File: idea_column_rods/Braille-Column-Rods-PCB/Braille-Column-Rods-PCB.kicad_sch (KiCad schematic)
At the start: 6 parts, among them J1 Conn_01x03, J5 Screw_Terminal_01x02, J6 Screw_Terminal_01x02

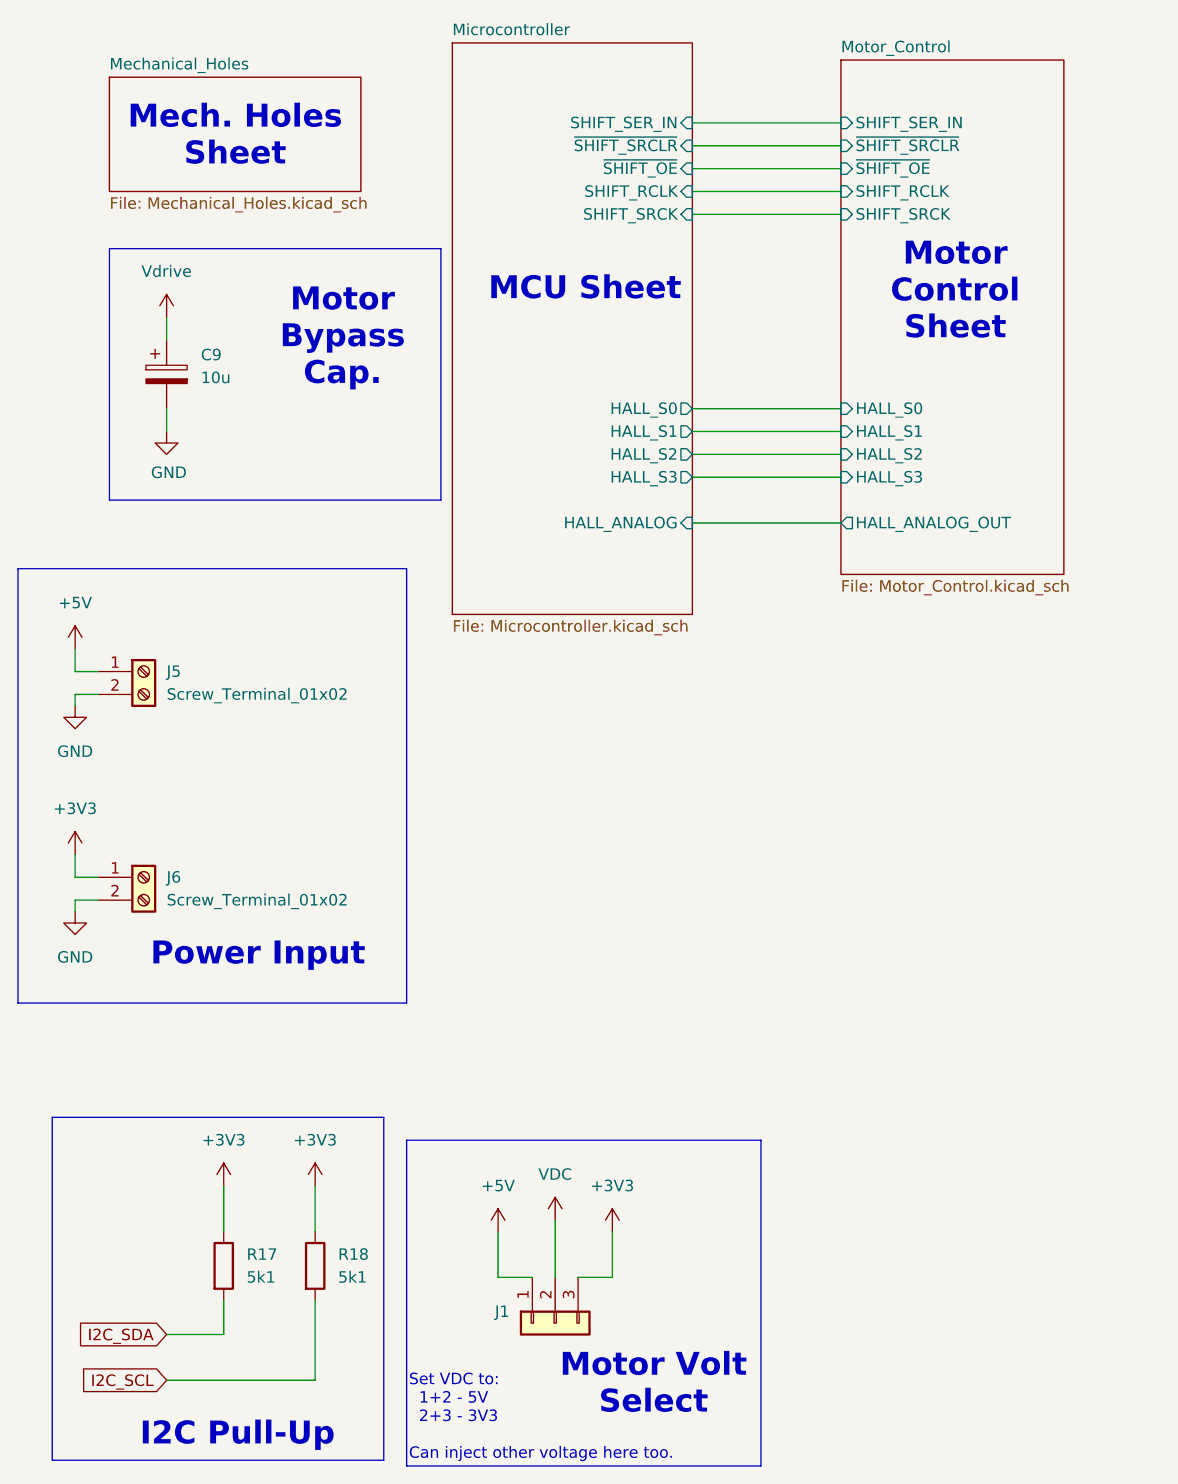
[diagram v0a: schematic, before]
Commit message: Create PCB and CAD for Type 4 Rev 1 rod cams (#13)
* WIP: Rods PCB placement

* WIP: Place the housing and motor X

* WIP: Position everything

* WIP: Update tight placement of DC motor

* WIP: Layout and route the stepper driver

* WIP: Motor layout is good

* WIP: Manual routing and silkscreens

* Comments

* Big routing

* Clean up DRC (mostly footprints)

* Fix spacing issue on top

* Fix spacing issues on bottom

* Create render of 6mm motor, add to PCB

* WIP: Get cams good

* WIP: Reorder the cam bushing and hall sensor

* Finish and tag release

* Complete type 4 rev 1

* Create dc_motor_clamp cad
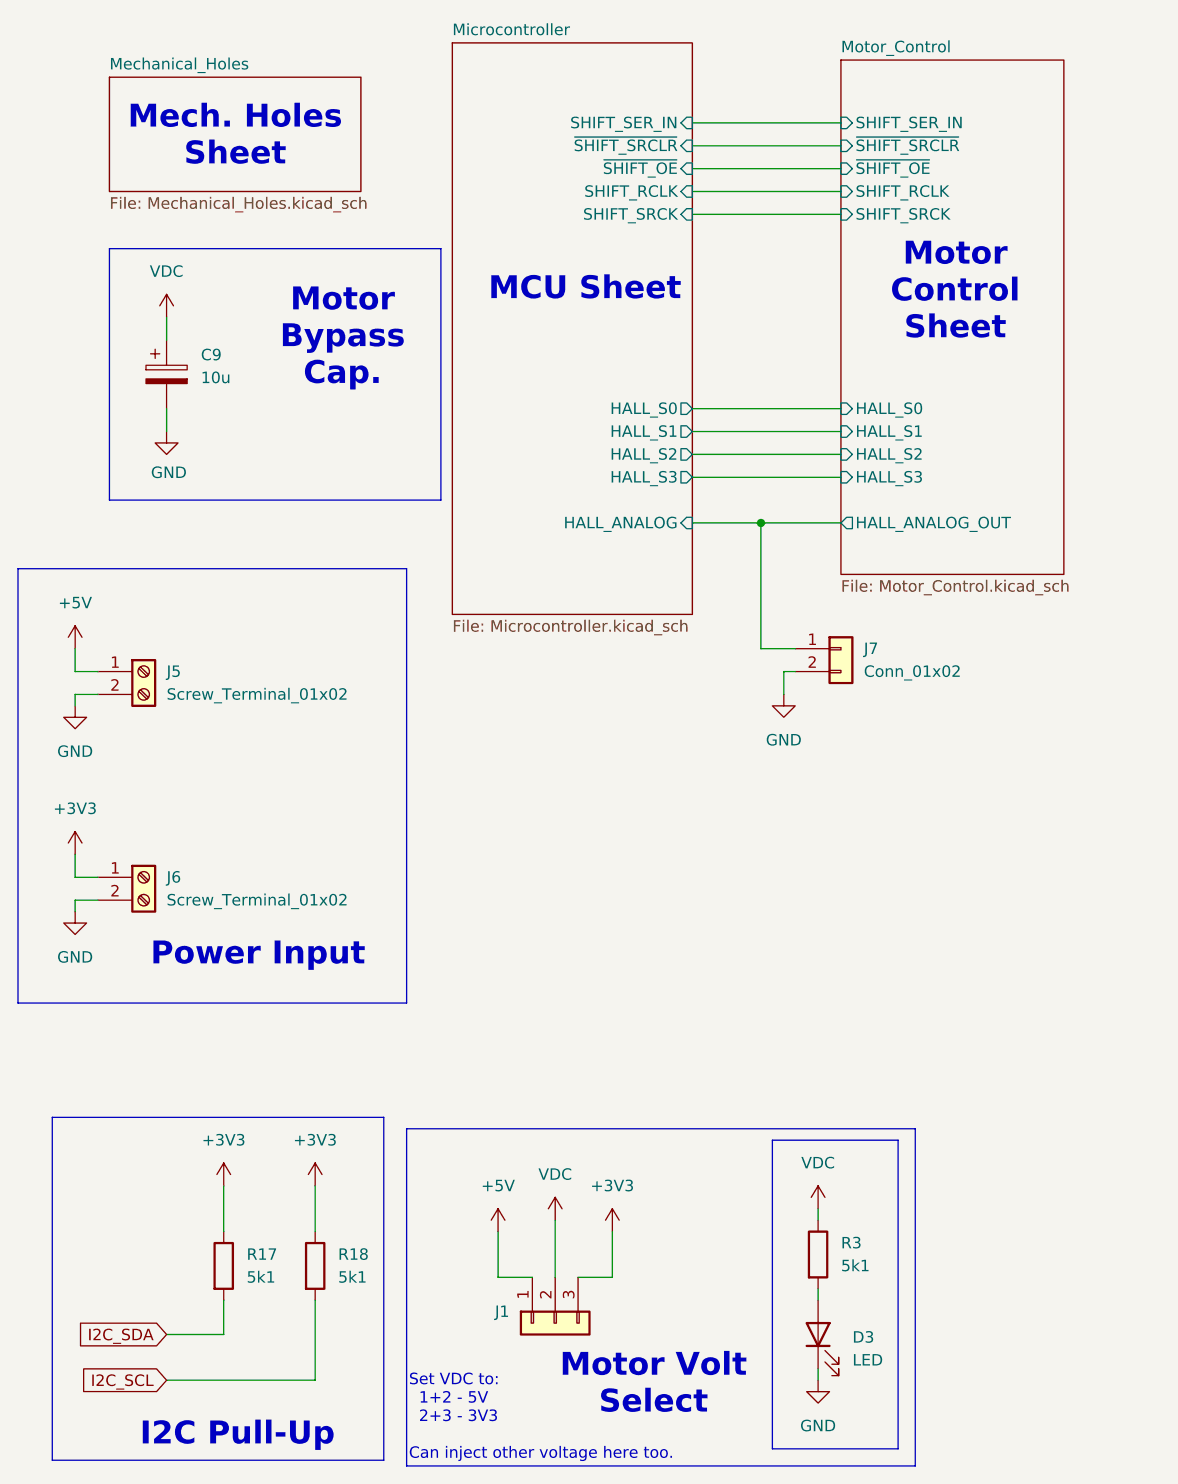
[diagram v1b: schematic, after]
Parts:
- added D3: LED, LED_SMD:LED_0603_1608Metric_Pad1.05x0.95mm_HandSolder, symbol Device:LED
- added J7: Conn_01x02, Connector_PinHeader_2.54mm:PinHeader_1x02_P2.54mm_Vertical, symbol Connector_Generic:Conn_01x02
- added R3: 5k1, Resistor_SMD:R_0603_1608Metric_Pad0.98x0.95mm_HandSolder, symbol Device:R
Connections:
- net Vdrive is gone; now on net VDC: C9.1
- net GND: now also D3.1 (K), J7.2 (Pin_2)
- net Microcontroller/HALL_ANALOG: now also J7.1 (Pin_1)
- net VDC: now also R3.1
- new net: D3.2 (A), R3.2
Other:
- title: (none) -> Braille Cam Rod Prototype (Type 4)
